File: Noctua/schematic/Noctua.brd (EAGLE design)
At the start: 30.6 x 62 mm, 45 parts, among them IC1 PCM3168A, U1 STM32F427V(100PIN), U4 LM3940IMP, X2 53048-05, Y2 8MHz

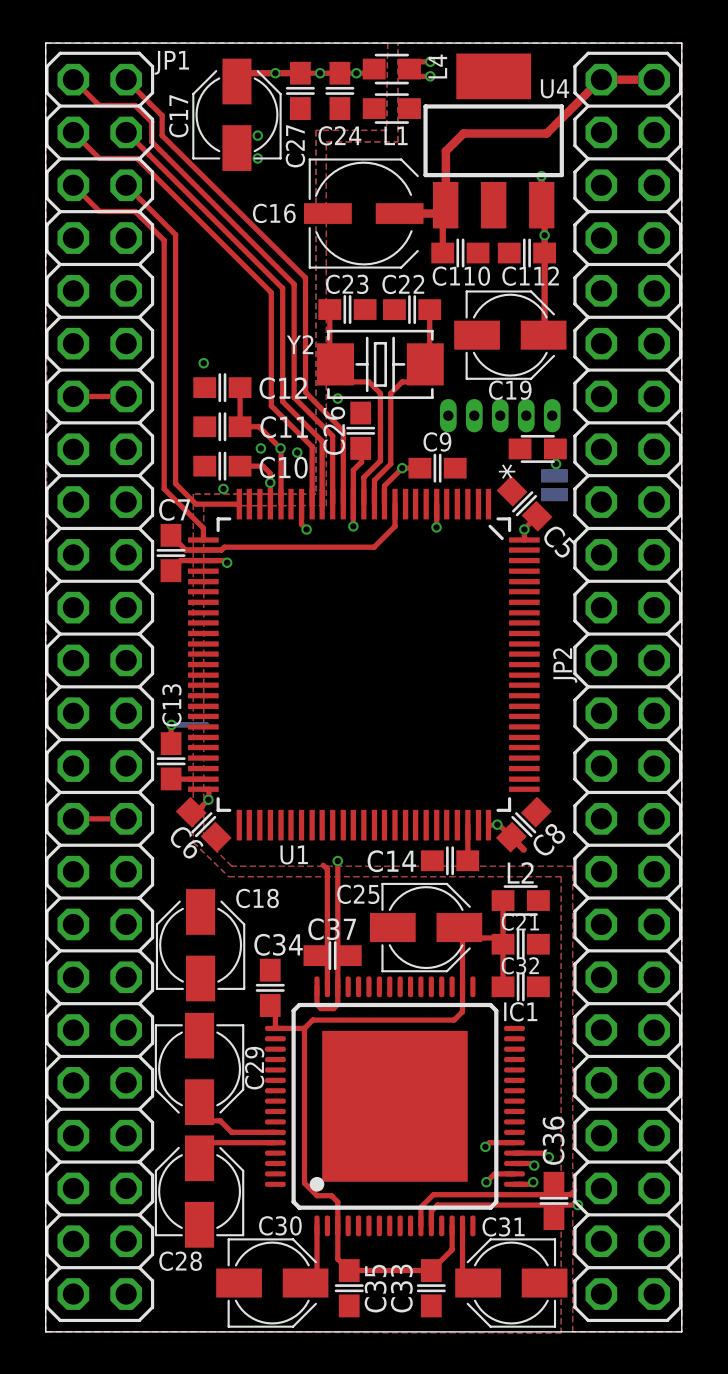
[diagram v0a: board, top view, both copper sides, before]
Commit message: Tracked all PCM analogue pins to headers
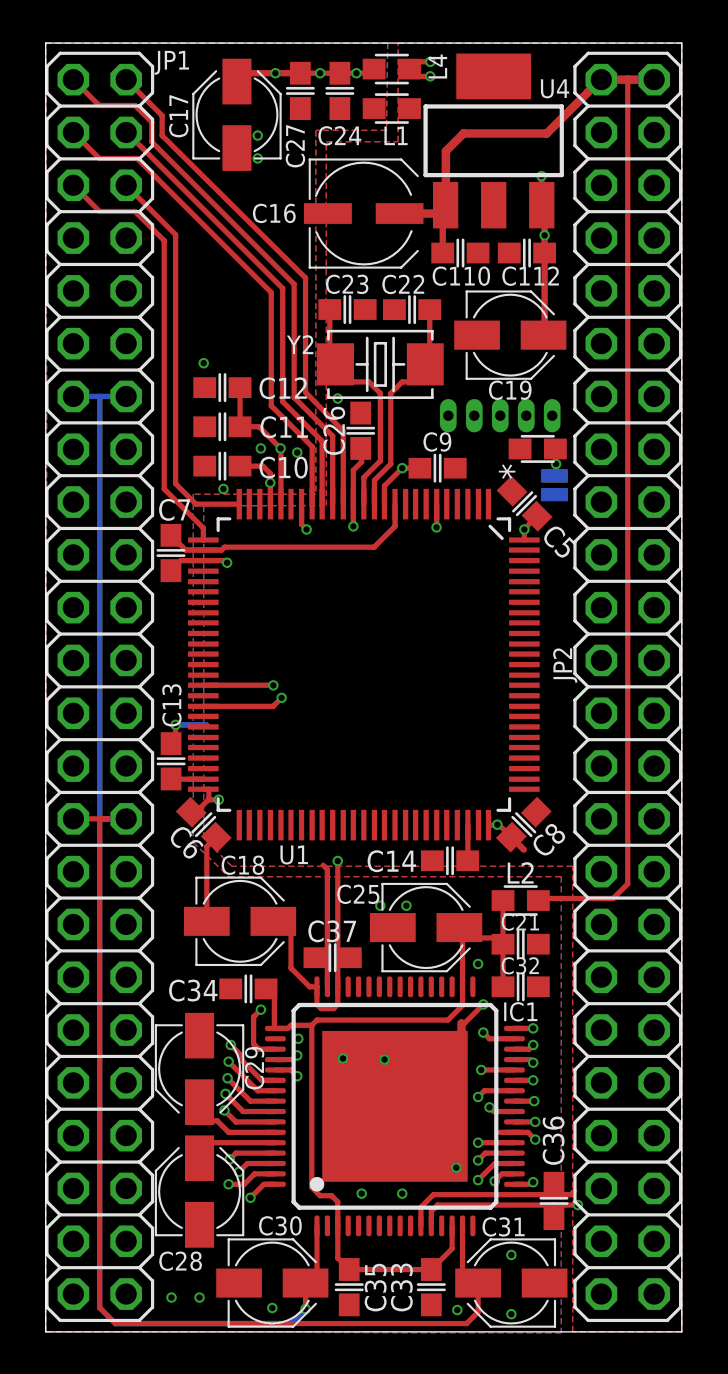
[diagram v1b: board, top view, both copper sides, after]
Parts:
- moved C18 2.22 mm to (9.35, 19.8), turned to 0 degrees
- moved C34 1.05 mm to (9.75, 16.5), turned to 180 degrees
- moved C37 0.10 mm to (13.8, 18.0)
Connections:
- removed net N$1: C31.+, IC1.15
- removed net N$5: C30.+, IC1.1
- net ADCREF: now also C30.+, IC1.1
- net DACREF: now also C31.+, IC1.15
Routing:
- net ADCREF: track 2.54 -> 61.1 mm, vias 0 -> 1
- net DACREF: track 2.54 -> 51.1 mm
- net +5V: track 18.5 -> 61.8 mm
- net AIN1+: track 0.00 -> 37.6 mm, vias 0 -> 1
- net AIN2+: track 0.00 -> 33.9 mm, vias 0 -> 1
- net AIN2-: track 0.00 -> 33.7 mm, vias 0 -> 1
- net AIN1-: track 0.00 -> 33.2 mm, vias 0 -> 1
- net AIN3+: track 0.00 -> 32.1 mm, vias 0 -> 1
- net AOUT4+: track 0.00 -> 31.8 mm, vias 0 -> 1
- net AIN5+: track 0.00 -> 31.3 mm, vias 0 -> 1
- net AOUT2+: track 0.00 -> 31.1 mm, vias 0 -> 1
- net AIN4+: track 0.00 -> 31.1 mm, vias 0 -> 1
- net AIN6+: track 0.00 -> 30.6 mm, vias 0 -> 1
- net AIN3-: track 0.00 -> 29.9 mm, vias 0 -> 1
- net AOUT5+: track 0.00 -> 29.8 mm, vias 0 -> 1
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
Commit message: some routing around MCU to finish and ADC serial connections to add
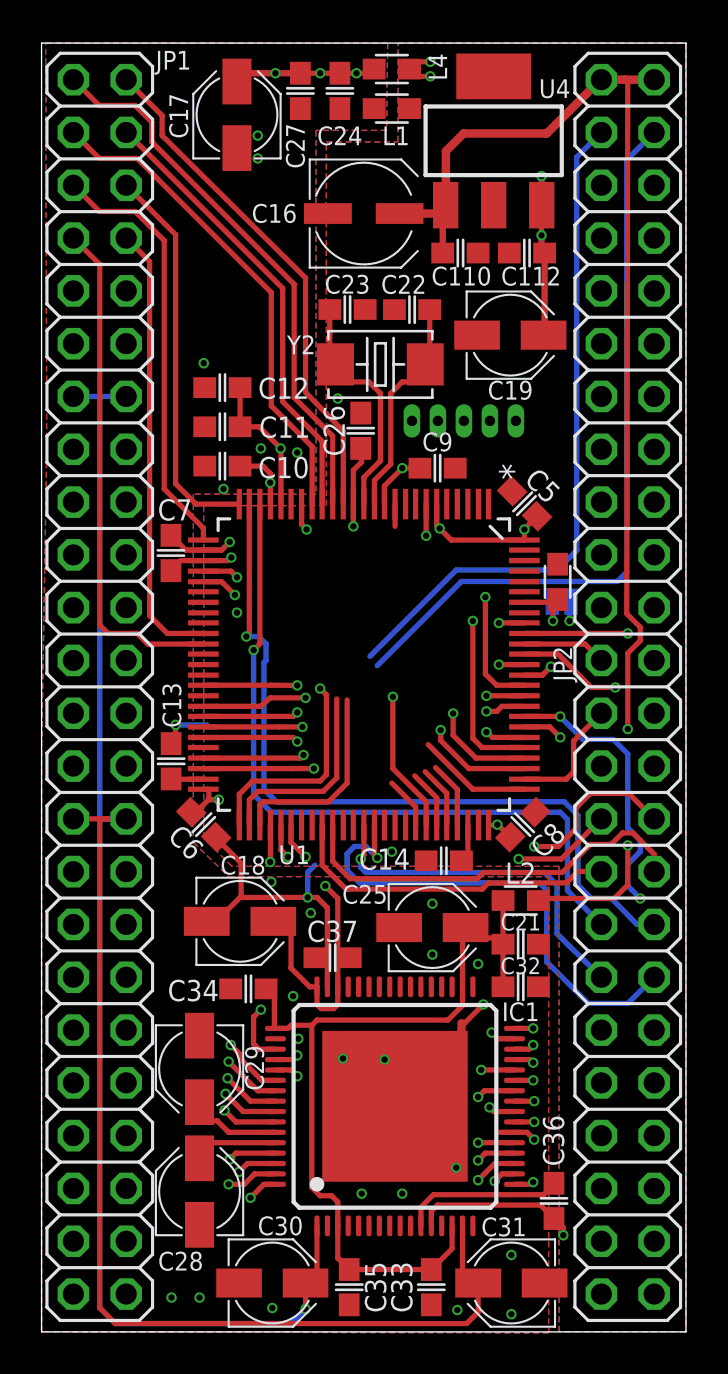
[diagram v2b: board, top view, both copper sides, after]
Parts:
- moved R3 6.47 mm to (24.6, 36.1), turned to 270 degrees
- moved BOOT 5.61 mm to (24.8, 35.1), turned to 0 degrees
- moved X2 1.77 mm to (20.1, 45.1)
- moved C14 0.30 mm to (19.1, 22.7)
- moved C25 0.30 mm to (18.6, 19.4)
- moved C8 0.05 mm to (22.9, 24.4)
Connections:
- removed net UART_RX: U1.69
- removed net UART_TX: U1.68
- net EXTI1: now also U1.92
- net EXTI2: now also U1.85
- net EXTI3: now also U1.83
- net EXTI4: now also U1.81
- net EXTI5: now also U1.7
- net EXTI6: now also U1.88
- net EXTI7: now also U1.84
- net EXTI8: now also U1.82
- net SPI2_MISO: now also U1.79
- net SPI2_MOSI: now also U1.80
- net SPI2_SCK: now also U1.78
- net SWCLK: now also U1.76
- net TIM1_CH1: now also U1.90; no longer U1.40
- net TIM1_CH2: now also U1.91; no longer U1.42
- net TIM2_CH1: now also U1.77
- net TIM2_CH2: now also U1.89
- net TIM3_CH1: now also U1.40
- net TIM3_CH2: now also U1.42
- net UART1_RX: now also U1.87; no longer U1.56
- net UART1_TX: now also U1.86; no longer U1.55
- net UART2_RX: now also U1.56
- net UART2_TX: now also U1.55
- net USBD_D+: now also U1.71
- net USBD_D-: now also U1.70
- net USBD_ID: now also U1.69
- net USBD_VBUS: now also U1.68
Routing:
- net USBH_VBUS: track 0.00 -> 45.2 mm
- net USBH_ID: track 0.00 -> 45.1 mm, vias 0 -> 1
- net I2C_SDA: track 0.00 -> 42.7 mm, vias 0 -> 1
- net I2C_SCL: track 0.00 -> 40.9 mm, vias 0 -> 1
- net USBH_D-: track 0.00 -> 40.7 mm
- net TIM5_CH2: track 0.00 -> 38.0 mm, vias 0 -> 1
- net TIM5_CH1: track 0.00 -> 35.4 mm, vias 0 -> 1
- net USBD_VBUS: track 0.00 -> 35.1 mm
- net USBH_D+: track 0.00 -> 34.1 mm, vias 0 -> 1
- net USBD_D+: track 0.00 -> 32.8 mm
- net USBD_ID: track 0.00 -> 32.6 mm, vias 0 -> 1
- net TIM3_CH2: track 0.00 -> 32.0 mm, vias 0 -> 2
- net SPI1_SCK: track 0.00 -> 30.9 mm, vias 0 -> 1
- net TIM3_CH1: track 0.00 -> 29.5 mm, vias 0 -> 2
- net USBD_D-: track 0.00 -> 29.1 mm
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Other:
- board size 30.6 x 62 mm -> 31 x 62 mm

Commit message: Most tracking complete. Only 2 SPI control lines left to add
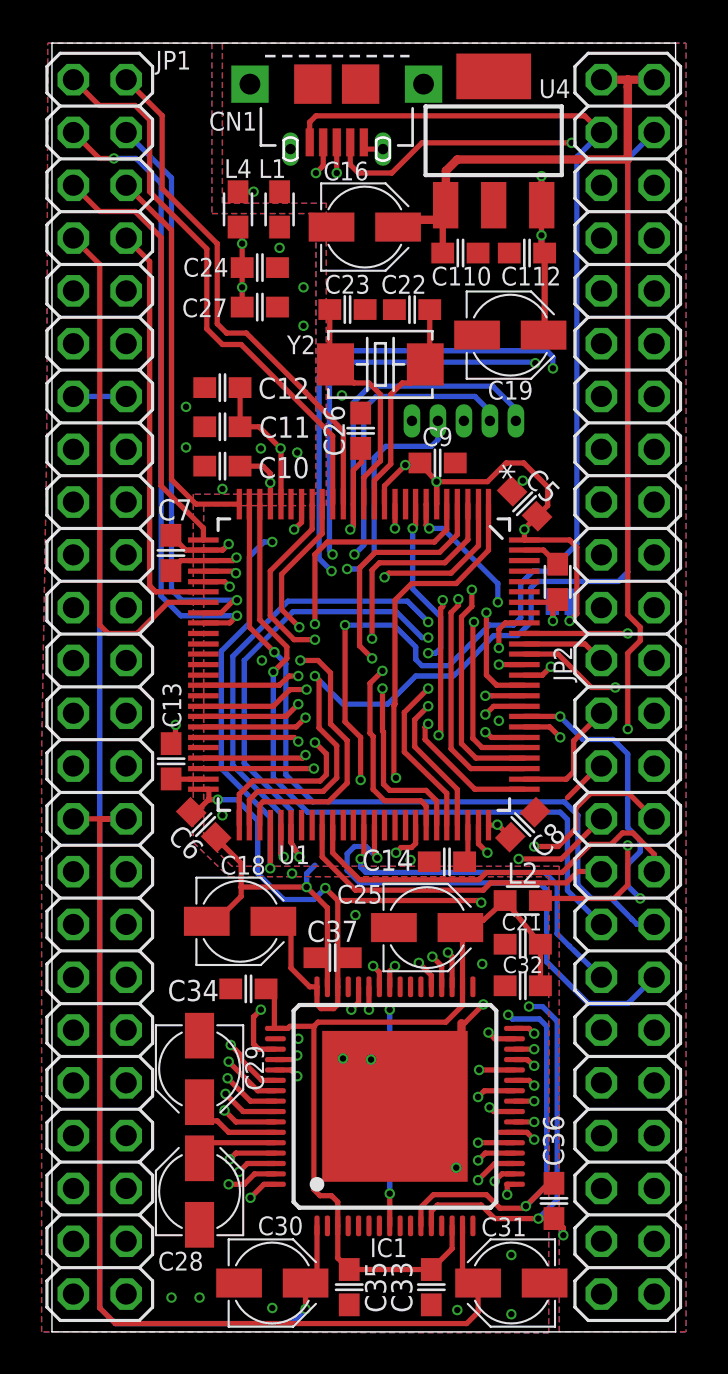
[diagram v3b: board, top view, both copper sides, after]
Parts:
- removed C17: 10uF, Rebel:PANASONIC_B
- added CN1: (no value), Rebel:HRS_ZX62RD-AB-5P8
- C16: device Rebel:CPOL-5 -> Rebel:PANASONIC_B
- moved C27 10.6 mm to (10.3, 49.3), turned to 0 degrees
- moved L4 10.0 mm to (9.25, 54.0), turned to 90 degrees
- moved C24 9.33 mm to (10.3, 51.2), turned to 0 degrees
- moved L1 7.26 mm to (11.2, 54.0), turned to 90 degrees
- moved C16 0.65 mm to (15.3, 53.1)
- moved C25 0.25 mm to (18.4, 19.4)
- moved C9 0.25 mm to (18.9, 41.8)
- moved C14 0.16 mm to (19.3, 22.6)
- moved C32 0.11 mm to (22.9, 16.6), turned to 180 degrees
- moved C21 0.10 mm to (22.9, 18.6), turned to 180 degrees
- moved L2 0.10 mm to (22.9, 20.8)
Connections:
- removed net N$4: U1.2
- removed net N$6: U1.3
- removed net N$7: U1.4
- removed net N$8: U1.5
- new net ADC_RST: IC1.4
- new net ADC_SPI_CLK: IC1.42, U1.84
- new net ADC_SPI_MISO: IC1.44, U1.17
- new net ADC_SPI_MOSI: IC1.43, U1.18
- new net ADC_SPI_NCS: IC1.45
- new net SAI_BCK: IC1.36, U1.4
- new net SAI_LRCK: IC1.35, U1.3
- new net SAI_SDI: IC1.8, U1.5
- new net SAI_SDO: IC1.37, U1.2
- net +A3V3: no longer C17.+
- net ADC2: now also U1.34; no longer U1.18
- net ADC4: now also U1.32; no longer U1.36
- net ADC6: now also U1.33; no longer U1.17
- net ADC8: now also U1.31; no longer U1.35
- net AGND: no longer C17.-
- net EXTI7: now also U1.8; no longer U1.84
- net GND: now also CN1.5, CN1.G, CN1.G2, CN1.G3, CN1.G4
- net SAI_MCLK: now also IC1.41
- net USBD_D+: now also CN1.3
- net USBD_D-: now also CN1.2
- net USBD_ID: now also CN1.4
- net USBD_VBUS: now also CN1.1
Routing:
- net SAI_SDI: track 0.00 -> 49.9 mm, vias 0 -> 3
- net +3V3: track 51.7 -> 101.3 mm, vias 14 -> 16
- net GND: track 32.4 -> 74.3 mm, vias 6 -> 11
- net ADC_SPI_MOSI: track 0.00 -> 36.6 mm, vias 0 -> 2
- net USBD_D-: track 29.1 -> 65.2 mm, vias 0 -> 4
- net ADC_SPI_MISO: track 0.00 -> 35.3 mm, vias 0 -> 2
- net USBD_VBUS: track 35.1 -> 65.4 mm, vias 0 -> 3
- net SAI_SDO: track 0.00 -> 29.5 mm, vias 0 -> 2
- net SAI_BCK: track 0.00 -> 29.3 mm, vias 0 -> 2
- net SAI_LRCK: track 0.00 -> 28.9 mm, vias 0 -> 2
- net SWDIO: track 3.21 -> 31.4 mm, vias 0 -> 2
- net SAI_MCLK: track 0.00 -> 28.1 mm, vias 0 -> 2
- net USBD_ID: track 32.6 -> 56.6 mm, vias 1 -> 2
- net UART2_RX: track 13.9 -> 37.2 mm, vias 1 -> 2
- net UART2_TX: track 13.0 -> 35.9 mm, vias 1 -> 2
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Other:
- board size 31 x 62 mm -> 30 x 62 mm

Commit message: Completed first draft of layout for review
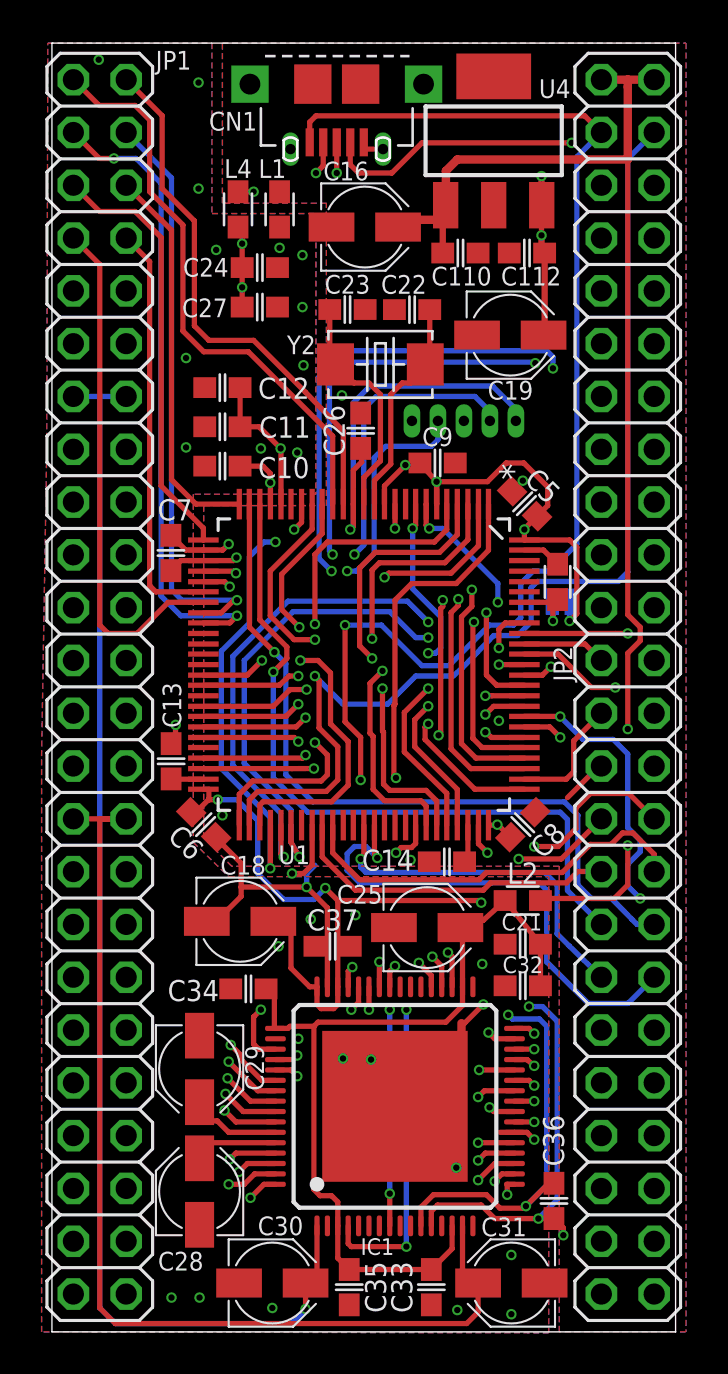
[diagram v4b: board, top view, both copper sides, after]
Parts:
- moved C37 0.55 mm to (13.8, 18.6)
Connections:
- net ADC_RST: now also U1.39
- net ADC_SPI_NCS: now also U1.58
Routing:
- net ADC_RST: track 0.00 -> 43.5 mm, vias 0 -> 3
- net ADC_SPI_NCS: track 0.00 -> 11.1 mm, vias 0 -> 2
- net ADC_SPI_MISO: track 35.3 -> 33.4 mm
- net ADC_SPI_MOSI: track 36.6 -> 34.7 mm
- net SAI_SDI: track 49.9 -> 48.2 mm
- net ADC1: track 27.1 -> 27.9 mm
- net ADC5: track 25.3 -> 26.0 mm
- net AGND: vias 21 -> 27
- added copper zone on layer 2, net AGND

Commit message: Tidied some tracks
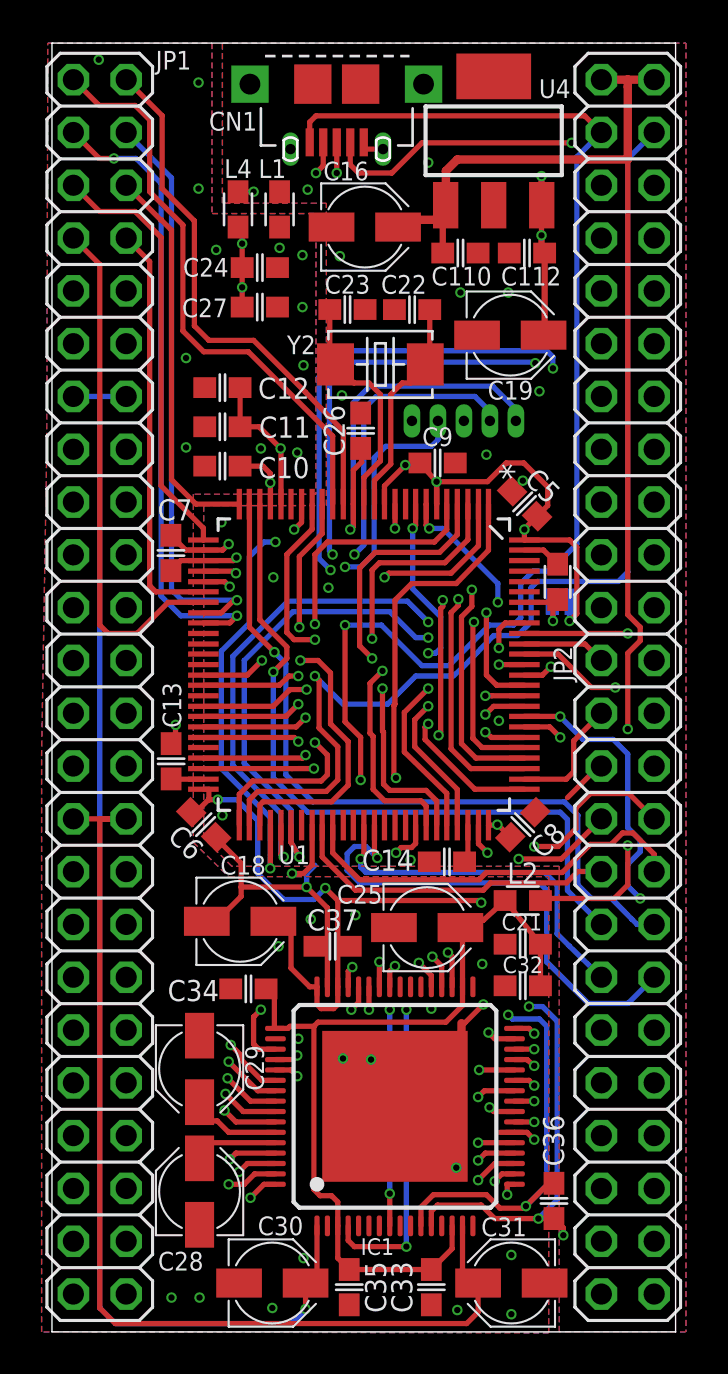
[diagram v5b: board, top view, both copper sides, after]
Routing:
- net DAC2: track 21.8 -> 19.2 mm
- net USBD_D-: track 65.2 -> 63.9 mm
- net USBH_D-: track 54.4 -> 53.3 mm
- net ADC_SPI_MISO: track 33.4 -> 32.7 mm
- net ADC_SPI_MOSI: track 34.7 -> 34.0 mm
- net GND: vias 11 -> 21
- net AGND: vias 27 -> 29
- added copper zone on layer 15, net AGND

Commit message: Noctua design checked and completed. Cube file updated to match assignments
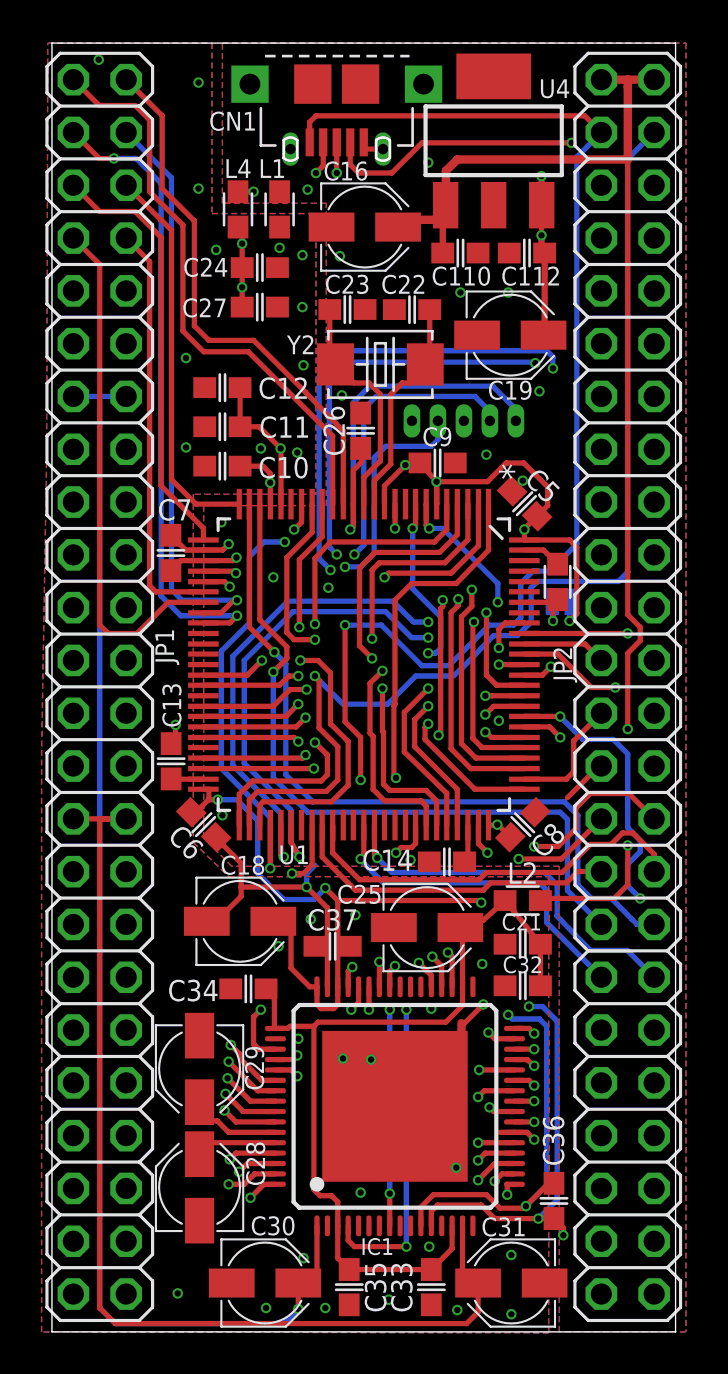
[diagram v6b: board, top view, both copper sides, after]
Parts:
- moved C30 0.35 mm to (10.6, 2.35)
- moved C28 0.20 mm to (7.40, 6.95)
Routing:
- net TIM6_CH2: track 24.2 -> 18.2 mm
- net TIM6_CH1: track 17.2 -> 16.6 mm
- net AGND: vias 29 -> 32
